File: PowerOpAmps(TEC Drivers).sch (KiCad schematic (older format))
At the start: 23 parts, among them U4 OPA569AIDWPR, U5 OPA569AIDWPR

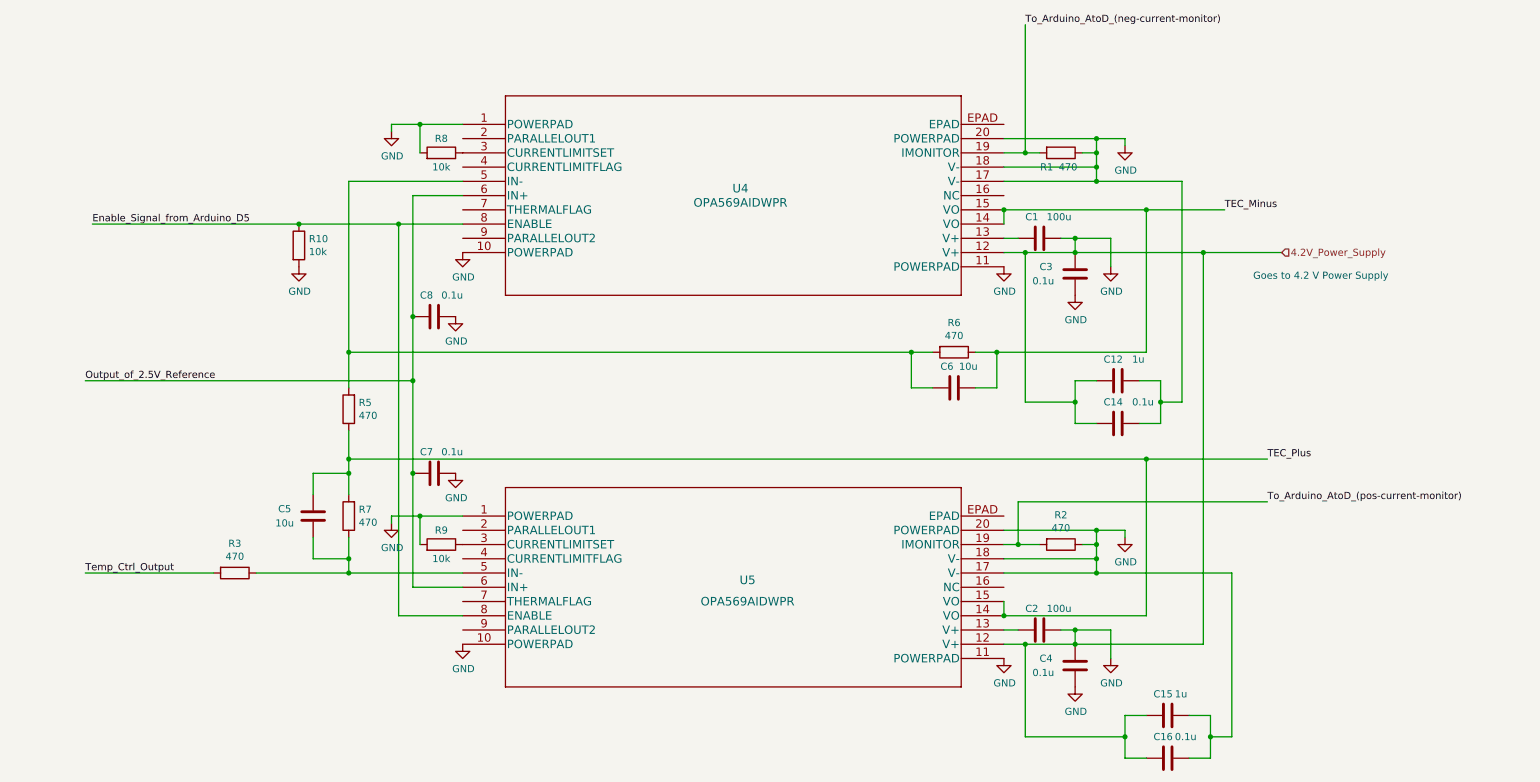
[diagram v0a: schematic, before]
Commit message: annotate all sheets
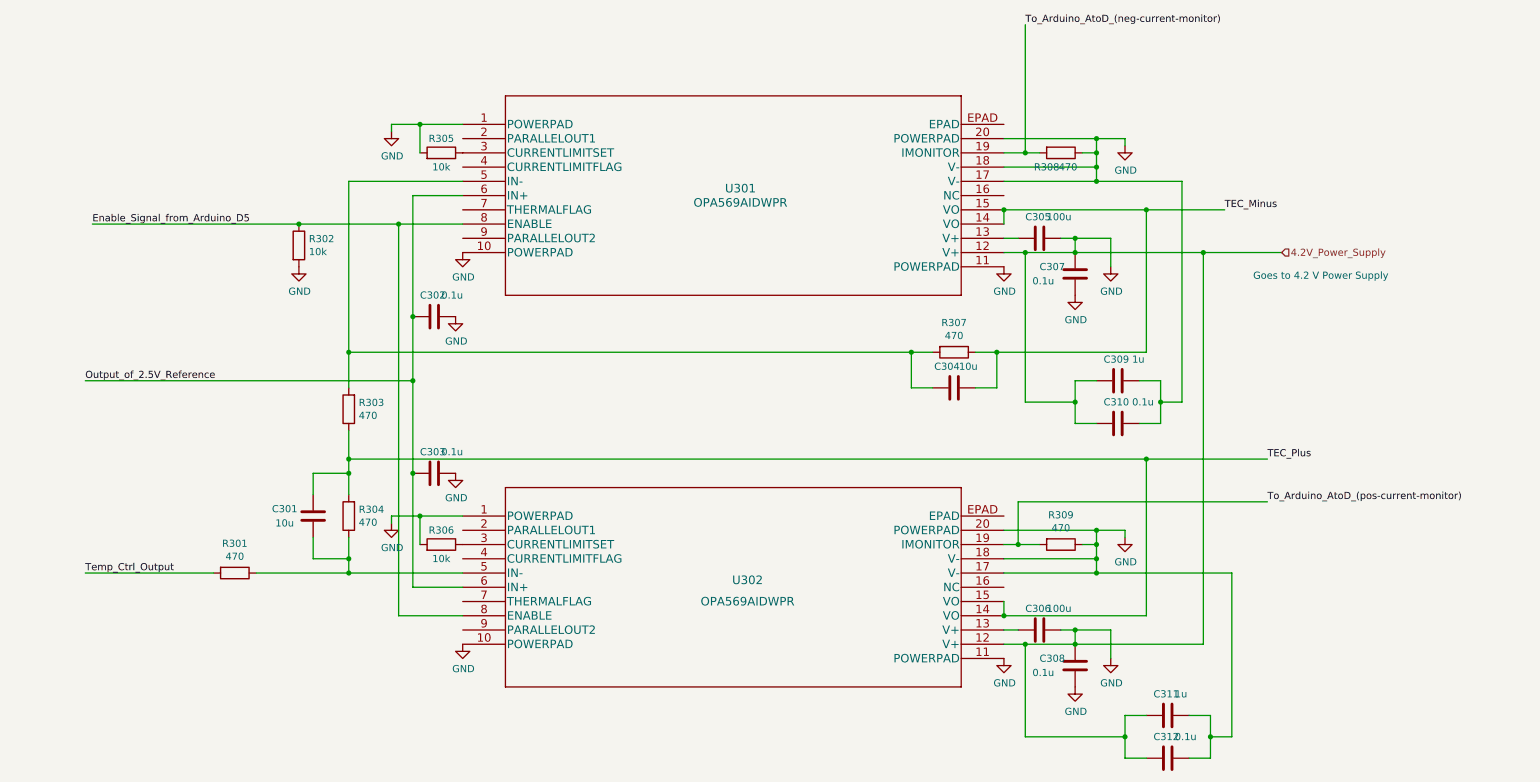
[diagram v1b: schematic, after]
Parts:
- renumbered C5 to C301, C8 to C302, C7 to C303, C6 to C304, C1 to C305, C2 to C306, C3 to C307, C4 to C308, C12 to C309, C14 to C310, C15 to C311, C16 to C312, R3 to R301, R10 to R302, R5 to R303, R7 to R304, R8 to R305, R9 to R306, R6 to R307, R1 to R308, R2 to R309, U4 to U301, U5 to U302
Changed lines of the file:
@@
 $EndDescr
 $Comp
-L OPA569AIDWPR:OPA569AIDWPR U5
+L OPA569AIDWPR:OPA569AIDWPR U302
 U 1 1 60C94364
 P 3700 4550
-F 0 "U5" H 5700 4100 60  0000 C CNN
+F 0 "U302" H 5700 4100 60  0000 C CNN
 F 1 "OPA569AIDWPR" H 5700 3950 60  0000 C CNN
 F 2 "DWP20_4P32X3P81" H 5600 4790 60  0001 C CNN
@@
 	3200 1800 3200 1850
 $Comp
-L power:GND #PWR018
+L power:GND #PWR0302
 U 1 1 60C996D8
 P 3200 1850
-F 0 "#PWR018" H 3200 1600 50  0001 C CNN
+F 0 "#PWR0302" H 3200 1600 50  0001 C CNN
 F 1 "GND" H 3205 1677 50  0000 C CNN
 F 2 "" H 3200 1850 50  0001 C CNN
@@
 	8150 2100 8150 2000
 $Comp
-L power:GND #PWR030
+L power:GND #PWR0314
 U 1 1 60C9A1CF
 P 8350 1950
-F 0 "#PWR030" H 8350 1700 50  0001 C CNN
+F 0 "#PWR0314" H 8350 1700 50  0001 C CNN
 F 1 "GND" H 8355 1777 50  0000 C CNN
 F 2 "" H 8350 1950 50  0001 C CNN
@@
 	8150 2000 8150 1900
 $Comp
-L Device:R R1
+L Device:R R308
 U 1 1 60C9D180
 P 7900 2000
-F 0 "R1" V 8000 1900 50  0000 C CNN
+F 0 "R308" V 8000 1900 50  0000 C CNN
 F 1 "470" V 8000 2050 50  0000 C CNN
 F 2 "" V 7830 2000 50  0001 C CNN
@@
 Connection ~ 8000 2600
 $Comp
-L power:GND #PWR026
+L power:GND #PWR0310
 U 1 1 60C9E215
 P 8000 3000
-F 0 "#PWR026" H 8000 2750 50  0001 C CNN
+F 0 "#PWR0310" H 8000 2750 50  0001 C CNN
 F 1 "GND" H 8005 2827 50  0000 C CNN
 F 2 "" H 8000 3000 50  0001 C CNN
@@
 $EndComp
 $Comp
-L power:GND #PWR028
+L power:GND #PWR0312
 U 1 1 60C9E30F
 P 8250 2800
-F 0 "#PWR028" H 8250 2550 50  0001 C CNN
+F 0 "#PWR0312" H 8250 2550 50  0001 C CNN
 F 1 "GND" H 8255 2627 50  0000 C CNN
 F 2 "" H 8250 2800 50  0001 C CNN
@@
 $EndComp
 $Comp
-L Device:C C3
+L Device:C C307
 U 1 1 60C9E72B
 P 8000 2850
-F 0 "C3" H 7750 2900 50  0000 L CNN
+F 0 "C307" H 7750 2900 50  0000 L CNN
 F 1 "0.1u" H 7700 2800 50  0000 L CNN
 F 2 "" H 8038 2700 50  0001 C CNN
@@
 Connection ~ 8000 2700
 $Comp
-L power:GND #PWR024
+L power:GND #PWR0308
 U 1 1 60C9EDCF
 P 7500 2800
-F 0 "#PWR024" H 7500 2550 50  0001 C CNN
+F 0 "#PWR0308" H 7500 2550 50  0001 C CNN
 F 1 "GND" H 7505 2627 50  0000 C CNN
 F 2 "" H 7500 2800 50  0001 C CNN
@@
 $EndComp
 $Comp
-L Device:C C1
+L Device:C C305
 U 1 1 60CA0405
 P 7750 2600
-F 0 "C1" V 7600 2500 50  0000 L CNN
+F 0 "C305" V 7600 2500 50  0000 L CNN
 F 1 "100u" V 7600 2650 50  0000 L CNN
 F 2 "" H 7788 2450 50  0001 C CNN
@@
 Connection ~ 8500 2400
 $Comp
-L Device:R R6
+L Device:R R307
 U 1 1 60CA6672
 P 7150 3400
-F 0 "R6" V 6943 3400 50  0000 C CNN
+F 0 "R307" V 6943 3400 50  0000 C CNN
 F 1 "470" V 7034 3400 50  0000 C CNN
 F 2 "" V 7080 3400 50  0001 C CNN
@@
 	7450 3400 7300 3400
 $Comp
-L Device:C C6
+L Device:C C304
 U 1 1 60CADB61
 P 7150 3650
-F 0 "C6" V 7000 3600 50  0000 C CNN
+F 0 "C304" V 7000 3600 50  0000 C CNN
 F 1 "10u" V 7000 3750 50  0000 C CNN
 F 2 "" H 7188 3500 50  0001 C CNN
@@
 Connection ~ 2900 3400
 $Comp
-L Device:R R5
+L Device:R R303
 U 1 1 60CAF386
 P 2900 3800
-F 0 "R5" H 2830 3754 50  0000 R CNN
+F 0 "R303" H 2830 3754 50  0000 R CNN
 F 1 "470" H 2830 3845 50  0000 R CNN
 F 2 "" V 2830 3800 50  0001 C CNN
@@
 	2650 4700 2650 4850
 $Comp
-L Device:C C5
+L Device:C C301
 U 1 1 60CB3BC7
 P 2650 4550
-F 0 "C5" H 2850 4500 50  0000 C CNN
+F 0 "C301" H 2850 4500 50  0000 C CNN
 F 1 "10u" H 2850 4600 50  0000 C CNN
 F 2 "" H 2688 4400 50  0001 C CNN
@@
 	2650 4400 2650 4250
 $Comp
-L Device:R R7
+L Device:R R304
 U 1 1 60CB4975
 P 2900 4550
-F 0 "R7" H 2830 4504 50  0000 R CNN
+F 0 "R304" H 2830 4504 50  0000 R CNN
 F 1 "470" H 2830 4595 50  0000 R CNN
 F 2 "" V 2830 4550 50  0001 C CNN
@@
 Connection ~ 2900 4950
 $Comp
-L Device:R R3
+L Device:R R301
 U 1 1 60CB799D
 P 2100 4950
-F 0 "R3" V 1893 4950 50  0000 C CNN
+F 0 "R301" V 1893 4950 50  0000 C CNN
 F 1 "470" V 1984 4950 50  0000 C CNN
 F 2 "" V 2030 4950 50  0001 C CNN
@@
 	3350 2300 3350 3150
 $Comp
-L Device:C C8
+L Device:C C302
 U 1 1 60CB9EEA
 P 3500 3150
-F 0 "C8" V 3350 3050 50  0000 L CNN
+F 0 "C302" V 3350 3050 50  0000 L CNN
 F 1 "0.1u" V 3350 3200 50  0000 L CNN
 F 2 "" H 3538 3000 50  0001 C CNN
@@
 Connection ~ 7500 2400
 $Comp
-L OPA569AIDWPR:OPA569AIDWPR U4
+L OPA569AIDWPR:OPA569AIDWPR U301
 U 1 1 60C92272
 P 3700 1800
-F 0 "U4" H 5650 1350 60  0000 C CNN
+F 0 "U301" H 5650 1350 60  0000 C CNN
 F 1 "OPA569AIDWPR" H 5650 1250 60  0000 C CNN
 F 2 "DWP20_4P32X3P81" H 5600 2040 60  0001 C CNN
@@
 $EndComp
 $Comp
-L power:GND #PWR020
+L power:GND #PWR0306
 U 1 1 60CB8330
 P 3700 2700
-F 0 "#PWR020" H 3700 2450 50  0001 C CNN
+F 0 "#PWR0306" H 3700 2450 50  0001 C CNN
 F 1 "GND" H 3705 2527 50  0000 C CNN
 F 2 "" H 3700 2700 50  0001 C CNN
@@
 	7500 2200 8150 2200
 $Comp
-L power:GND #PWR021
+L power:GND #PWR0304
 U 1 1 60CBC7D5
 P 3650 3150
-F 0 "#PWR021" H 3650 2900 50  0001 C CNN
+F 0 "#PWR0304" H 3650 2900 50  0001 C CNN
 F 1 "GND" H 3655 2977 50  0000 C CNN
 F 2 "" H 3650 3150 50  0001 C CNN
@@
 $EndComp
 $Comp
-L Device:C C7
+L Device:C C303
 U 1 1 60C859CC
 P 3500 4250
-F 0 "C7" V 3350 4150 50  0000 L CNN
+F 0 "C303" V 3350 4150 50  0000 L CNN
 F 1 "0.1u" V 3350 4300 50  0000 L CNN
 F 2 "" H 3538 4100 50  0001 C CNN
@@
 $EndComp
 $Comp
-L power:GND #PWR022
+L power:GND #PWR0305
 U 1 1 60C85B5A
 P 3650 4250
-F 0 "#PWR022" H 3650 4000 50  0001 C CNN
+F 0 "#PWR0305" H 3650 4000 50  0001 C CNN
 F 1 "GND" H 3655 4077 50  0000 C CNN
 F 2 "" H 3650 4250 50  0001 C CNN
@@
 Connection ~ 8000 5350
 $Comp
-L power:GND #PWR027
+L power:GND #PWR0311
 U 1 1 60C89B9A
 P 8000 5750
-F 0 "#PWR027" H 8000 5500 50  0001 C CNN
+F 0 "#PWR0311" H 8000 5500 50  0001 C CNN
 F 1 "GND" H 8005 5577 50  0000 C CNN
 F 2 "" H 8000 5750 50  0001 C CNN
@@
 $EndComp
 $Comp
-L power:GND #PWR029
+L power:GND #PWR0313
 U 1 1 60C89BA4
 P 8250 5550
-F 0 "#PWR029" H 8250 5300 50  0001 C CNN
+F 0 "#PWR0313" H 8250 5300 50  0001 C CNN
 F 1 "GND" H 8255 5377 50  0000 C CNN
 F 2 "" H 8250 5550 50  0001 C CNN
@@
 $EndComp
 $Comp
-L Device:C C4
+L Device:C C308
 U 1 1 60C89BAE
 P 8000 5600
-F 0 "C4" H 7750 5650 50  0000 L CNN
+F 0 "C308" H 7750 5650 50  0000 L CNN
 F 1 "0.1u" H 7700 5550 50  0000 L CNN
 F 2 "" H 8038 5450 50  0001 C CNN
@@
 Connection ~ 8000 5450
 $Comp
-L Device:C C2
+L Device:C C306
 U 1 1 60C89BB9
 P 7750 5350
-F 0 "C2" V 7600 5250 50  0000 L CNN
+F 0 "C306" V 7600 5250 50  0000 L CNN
 F 1 "100u" V 7600 5400 50  0000 L CNN
 F 2 "" H 7788 5200 50  0001 C CNN
@@
 	8900 5450 8900 2700
 $Comp
-L power:GND #PWR025
+L power:GND #PWR0309
 U 1 1 60C94EDB
 P 7500 5550
-F 0 "#PWR025" H 7500 5300 50  0001 C CNN
+F 0 "#PWR0309" H 7500 5300 50  0001 C CNN
 F 1 "GND" H 7505 5377 50  0000 C CNN
 F 2 "" H 7500 5550 50  0001 C CNN
@@
 	8150 4850 8150 4750
 $Comp
-L power:GND #PWR031
+L power:GND #PWR0315
 U 1 1 60C9936E
 P 8350 4700
-F 0 "#PWR031" H 8350 4450 50  0001 C CNN
+F 0 "#PWR0315" H 8350 4450 50  0001 C CNN
 F 1 "GND" H 8355 4527 50  0000 C CNN
 F 2 "" H 8350 4700 50  0001 C CNN
@@
 	8150 4750 8150 4650
 $Comp
-L Device:R R2
+L Device:R R309
 U 1 1 60C9937F
 P 7900 4750
-F 0 "R2" V 7693 4750 50  0000 C CNN
+F 0 "R309" V 7693 4750 50  0000 C CNN
 F 1 "470" V 7784 4750 50  0000 C CNN
 F 2 "" V 7830 4750 50  0001 C CNN
@@
 Enable_Signal_from_Arduino_D5
 $Comp
-L Device:R R10
+L Device:R R302
 U 1 1 60CB8623
 P 2550 2650
-F 0 "R10" H 2620 2696 50  0000 L CNN
+F 0 "R302" H 2620 2696 50  0000 L CNN
 F 1 "10k" H 2620 2605 50  0000 L CNN
 F 2 "" V 2480 2650 50  0001 C CNN
@@
 	2550 2500 1100 2500
 $Comp
-L power:GND #PWR017
+L power:GND #PWR0301
 U 1 1 60CB8F3D
 P 2550 2800
-F 0 "#PWR017" H 2550 2550 50  0001 C CNN
+F 0 "#PWR0301" H 2550 2550 50  0001 C CNN
 F 1 "GND" H 2555 2627 50  0000 C CNN
 F 2 "" H 2550 2800 50  0001 C CNN
@@
 $EndComp
 $Comp
-L power:GND #PWR023
+L power:GND #PWR0307
 U 1 1 60CB936E
 P 3700 5450
-F 0 "#PWR023" H 3700 5200 50  0001 C CNN
+F 0 "#PWR0307" H 3700 5200 50  0001 C CNN
 F 1 "GND" H 3705 5277 50  0000 C CNN
 F 2 "" H 3700 5450 50  0001 C CNN
@@
 	7650 5450 8000 5450
 $Comp
-L Device:C C15
+L Device:C C311
 U 1 1 60CD3EBB
 P 8650 5950
-F 0 "C15" V 8500 5850 50  0000 L CNN
+F 0 "C311" V 8500 5850 50  0000 L CNN
 F 1 "1u" V 8500 6000 50  0000 L CNN
 F 2 "" H 8688 5800 50  0001 C CNN
@@
 $EndComp
 $Comp
-L Device:C C16
+L Device:C C312
 U 1 1 60CD4799
 P 8650 6250
-F 0 "C16" V 8500 6150 50  0000 L CNN
+F 0 "C312" V 8500 6150 50  0000 L CNN
 F 1 "0.1u" V 8500 6300 50  0000 L CNN
 F 2 "" H 8688 6100 50  0001 C CNN
@@
 	8000 3600 8150 3600
 $Comp
-L Device:C C12
+L Device:C C309
 U 1 1 60CDE792
 P 8300 3600
-F 0 "C12" V 8150 3500 50  0000 L CNN
+F 0 "C309" V 8150 3500 50  0000 L CNN
 F 1 "1u" V 8150 3700 50  0000 L CNN
 F 2 "" H 8338 3450 50  0001 C CNN
@@
 $EndComp
 $Comp
-L Device:C C14
+L Device:C C310
 U 1 1 60CDE79C
 P 8300 3900
-F 0 "C14" V 8150 3800 50  0000 L CNN
+F 0 "C310" V 8150 3800 50  0000 L CNN
 F 1 "0.1u" V 8150 4000 50  0000 L CNN
 F 2 "" H 8338 3750 50  0001 C CNN
@@
 	3400 1800 3700 1800
 $Comp
-L Device:R R8
+L Device:R R305
 U 1 1 60DF1308
 P 3550 2000
-F 0 "R8" V 3650 2000 50  0000 C CNN
+F 0 "R305" V 3650 2000 50  0000 C CNN
 F 1 "10k" V 3450 2000 50  0000 C CNN
 F 2 "" V 3480 2000 50  0001 C CNN
@@
 	3200 4550 3200 4600
 $Comp
-L power:GND #PWR?
+L power:GND #PWR0303
 U 1 1 60E59C67
 P 3200 4600
-F 0 "#PWR?" H 3200 4350 50  0001 C CNN
+F 0 "#PWR0303" H 3200 4350 50  0001 C CNN
 F 1 "GND" H 3205 4427 50  0000 C CNN
 F 2 "" H 3200 4600 50  0001 C CNN
@@
 	3400 4550 3700 4550
 $Comp
-L Device:R R9
+L Device:R R306
 U 1 1 60E59C71
 P 3550 4750
-F 0 "R9" V 3650 4750 50  0000 C CNN
+F 0 "R306" V 3650 4750 50  0000 C CNN
 F 1 "10k" V 3450 4750 50  0000 C CNN
 F 2 "" V 3480 4750 50  0001 C CNN

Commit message: add footprints 2 julia
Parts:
- U301, U302: footprint DWP20_4P32X3P81 -> footprint libraries:OPA569AIDWPR
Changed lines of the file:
@@
 F 0 "U302" H 5700 4100 60  0000 C CNN
 F 1 "OPA569AIDWPR" H 5700 3950 60  0000 C CNN
-F 2 "DWP20_4P32X3P81" H 5600 4790 60  0001 C CNN
+F 2 "footprint libraries:OPA569AIDWPR" H 5600 4790 60  0001 C CNN
 F 3 "" H 3700 4550 60  0000 C CNN
 	1    3700 4550
@@
 F 0 "U301" H 5650 1350 60  0000 C CNN
 F 1 "OPA569AIDWPR" H 5650 1250 60  0000 C CNN
-F 2 "DWP20_4P32X3P81" H 5600 2040 60  0001 C CNN
+F 2 "footprint libraries:OPA569AIDWPR" H 5600 2040 60  0001 C CNN
 F 3 "" H 3700 1800 60  0000 C CNN
 	1    3700 1800

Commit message: added vishay dude & capacitor & resistor footprints
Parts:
- C301, C302, C303, C304, C305, C306, C307, C308, C309, C310, C311, C312: footprint (none) -> Capacitor_SMD:C_0402_1005Metric
- R301, R302, R303, R304, R305, R306, R307, R308, R309: footprint (none) -> Resistor_SMD:R_0402_1005Metric
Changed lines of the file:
@@
 F 0 "R308" V 8000 1900 50  0000 C CNN
 F 1 "470" V 8000 2050 50  0000 C CNN
-F 2 "" V 7830 2000 50  0001 C CNN
+F 2 "Resistor_SMD:R_0402_1005Metric" V 7830 2000 50  0001 C CNN
 F 3 "~" H 7900 2000 50  0001 C CNN
 	1    7900 2000
@@
 F 0 "C307" H 7750 2900 50  0000 L CNN
 F 1 "0.1u" H 7700 2800 50  0000 L CNN
-F 2 "" H 8038 2700 50  0001 C CNN
+F 2 "Capacitor_SMD:C_0402_1005Metric" H 8038 2700 50  0001 C CNN
 F 3 "~" H 8000 2850 50  0001 C CNN
 	1    8000 2850
@@
 F 0 "C305" V 7600 2500 50  0000 L CNN
 F 1 "100u" V 7600 2650 50  0000 L CNN
-F 2 "" H 7788 2450 50  0001 C CNN
+F 2 "Capacitor_SMD:C_0402_1005Metric" H 7788 2450 50  0001 C CNN
 F 3 "~" H 7750 2600 50  0001 C CNN
 	1    7750 2600
@@
 F 0 "R307" V 6943 3400 50  0000 C CNN
 F 1 "470" V 7034 3400 50  0000 C CNN
-F 2 "" V 7080 3400 50  0001 C CNN
+F 2 "Resistor_SMD:R_0402_1005Metric" V 7080 3400 50  0001 C CNN
 F 3 "~" H 7150 3400 50  0001 C CNN
 	1    7150 3400
@@
 F 0 "C304" V 7000 3600 50  0000 C CNN
 F 1 "10u" V 7000 3750 50  0000 C CNN
-F 2 "" H 7188 3500 50  0001 C CNN
+F 2 "Capacitor_SMD:C_0402_1005Metric" H 7188 3500 50  0001 C CNN
 F 3 "~" H 7150 3650 50  0001 C CNN
 	1    7150 3650
@@
 F 0 "R303" H 2830 3754 50  0000 R CNN
 F 1 "470" H 2830 3845 50  0000 R CNN
-F 2 "" V 2830 3800 50  0001 C CNN
+F 2 "Resistor_SMD:R_0402_1005Metric" V 2830 3800 50  0001 C CNN
 F 3 "~" H 2900 3800 50  0001 C CNN
 	1    2900 3800
@@
 F 0 "C301" H 2850 4500 50  0000 C CNN
 F 1 "10u" H 2850 4600 50  0000 C CNN
-F 2 "" H 2688 4400 50  0001 C CNN
+F 2 "Capacitor_SMD:C_0402_1005Metric" H 2688 4400 50  0001 C CNN
 F 3 "~" H 2650 4550 50  0001 C CNN
 	1    2650 4550
@@
 F 0 "R304" H 2830 4504 50  0000 R CNN
 F 1 "470" H 2830 4595 50  0000 R CNN
-F 2 "" V 2830 4550 50  0001 C CNN
+F 2 "Resistor_SMD:R_0402_1005Metric" V 2830 4550 50  0001 C CNN
 F 3 "~" H 2900 4550 50  0001 C CNN
 	1    2900 4550
@@
 F 0 "R301" V 1893 4950 50  0000 C CNN
 F 1 "470" V 1984 4950 50  0000 C CNN
-F 2 "" V 2030 4950 50  0001 C CNN
+F 2 "Resistor_SMD:R_0402_1005Metric" V 2030 4950 50  0001 C CNN
 F 3 "~" H 2100 4950 50  0001 C CNN
 	1    2100 4950
@@
 F 0 "C302" V 3350 3050 50  0000 L CNN
 F 1 "0.1u" V 3350 3200 50  0000 L CNN
-F 2 "" H 3538 3000 50  0001 C CNN
+F 2 "Capacitor_SMD:C_0402_1005Metric" H 3538 3000 50  0001 C CNN
 F 3 "~" H 3500 3150 50  0001 C CNN
 	1    3500 3150
@@
 F 0 "C303" V 3350 4150 50  0000 L CNN
 F 1 "0.1u" V 3350 4300 50  0000 L CNN
-F 2 "" H 3538 4100 50  0001 C CNN
+F 2 "Capacitor_SMD:C_0402_1005Metric" H 3538 4100 50  0001 C CNN
 F 3 "~" H 3500 4250 50  0001 C CNN
 	1    3500 4250
@@
 F 0 "C308" H 7750 5650 50  0000 L CNN
 F 1 "0.1u" H 7700 5550 50  0000 L CNN
-F 2 "" H 8038 5450 50  0001 C CNN
+F 2 "Capacitor_SMD:C_0402_1005Metric" H 8038 5450 50  0001 C CNN
 F 3 "~" H 8000 5600 50  0001 C CNN
 	1    8000 5600
@@
 F 0 "C306" V 7600 5250 50  0000 L CNN
 F 1 "100u" V 7600 5400 50  0000 L CNN
-F 2 "" H 7788 5200 50  0001 C CNN
+F 2 "Capacitor_SMD:C_0402_1005Metric" H 7788 5200 50  0001 C CNN
 F 3 "~" H 7750 5350 50  0001 C CNN
 	1    7750 5350
@@
 F 0 "R309" V 7693 4750 50  0000 C CNN
 F 1 "470" V 7784 4750 50  0000 C CNN
-F 2 "" V 7830 4750 50  0001 C CNN
+F 2 "Resistor_SMD:R_0402_1005Metric" V 7830 4750 50  0001 C CNN
 F 3 "~" H 7900 4750 50  0001 C CNN
 	1    7900 4750
@@
 F 0 "R302" H 2620 2696 50  0000 L CNN
 F 1 "10k" H 2620 2605 50  0000 L CNN
-F 2 "" V 2480 2650 50  0001 C CNN
+F 2 "Resistor_SMD:R_0402_1005Metric" V 2480 2650 50  0001 C CNN
 F 3 "~" H 2550 2650 50  0001 C CNN
 	1    2550 2650
@@
 F 0 "C311" V 8500 5850 50  0000 L CNN
 F 1 "1u" V 8500 6000 50  0000 L CNN
-F 2 "" H 8688 5800 50  0001 C CNN
+F 2 "Capacitor_SMD:C_0402_1005Metric" H 8688 5800 50  0001 C CNN
 F 3 "~" H 8650 5950 50  0001 C CNN
 	1    8650 5950
@@
 F 0 "C312" V 8500 6150 50  0000 L CNN
 F 1 "0.1u" V 8500 6300 50  0000 L CNN
-F 2 "" H 8688 6100 50  0001 C CNN
+F 2 "Capacitor_SMD:C_0402_1005Metric" H 8688 6100 50  0001 C CNN
 F 3 "~" H 8650 6250 50  0001 C CNN
 	1    8650 6250
@@
 F 0 "C309" V 8150 3500 50  0000 L CNN
 F 1 "1u" V 8150 3700 50  0000 L CNN
-F 2 "" H 8338 3450 50  0001 C CNN
+F 2 "Capacitor_SMD:C_0402_1005Metric" H 8338 3450 50  0001 C CNN
 F 3 "~" H 8300 3600 50  0001 C CNN
 	1    8300 3600
@@
 F 0 "C310" V 8150 3800 50  0000 L CNN
 F 1 "0.1u" V 8150 4000 50  0000 L CNN
-F 2 "" H 8338 3750 50  0001 C CNN
+F 2 "Capacitor_SMD:C_0402_1005Metric" H 8338 3750 50  0001 C CNN
 F 3 "~" H 8300 3900 50  0001 C CNN
 	1    8300 3900
@@
 F 0 "R305" V 3650 2000 50  0000 C CNN
 F 1 "10k" V 3450 2000 50  0000 C CNN
-F 2 "" V 3480 2000 50  0001 C CNN
+F 2 "Resistor_SMD:R_0402_1005Metric" V 3480 2000 50  0001 C CNN
 F 3 "~" H 3550 2000 50  0001 C CNN
 	1    3550 2000
@@
 F 0 "R306" V 3650 4750 50  0000 C CNN
 F 1 "10k" V 3450 4750 50  0000 C CNN
-F 2 "" V 3480 4750 50  0001 C CNN
+F 2 "Resistor_SMD:R_0402_1005Metric" V 3480 4750 50  0001 C CNN
 F 3 "~" H 3550 4750 50  0001 C CNN
 	1    3550 4750

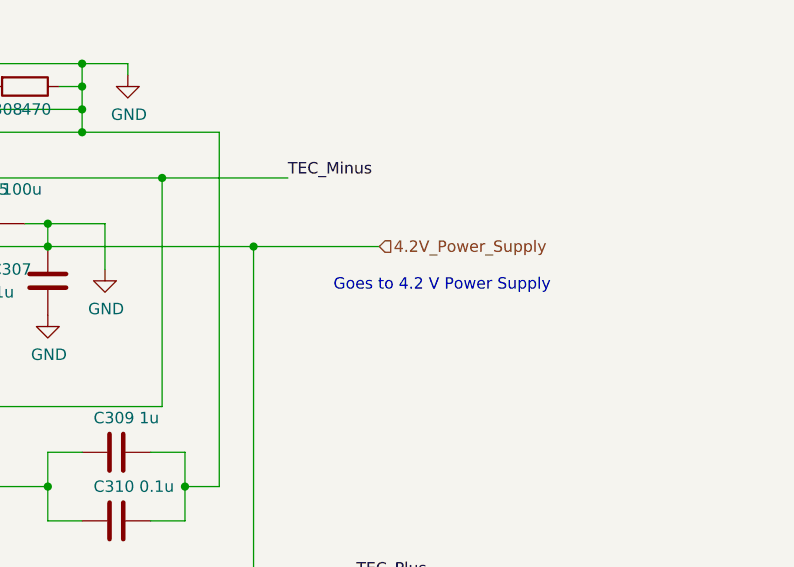
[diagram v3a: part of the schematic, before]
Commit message: added more ports
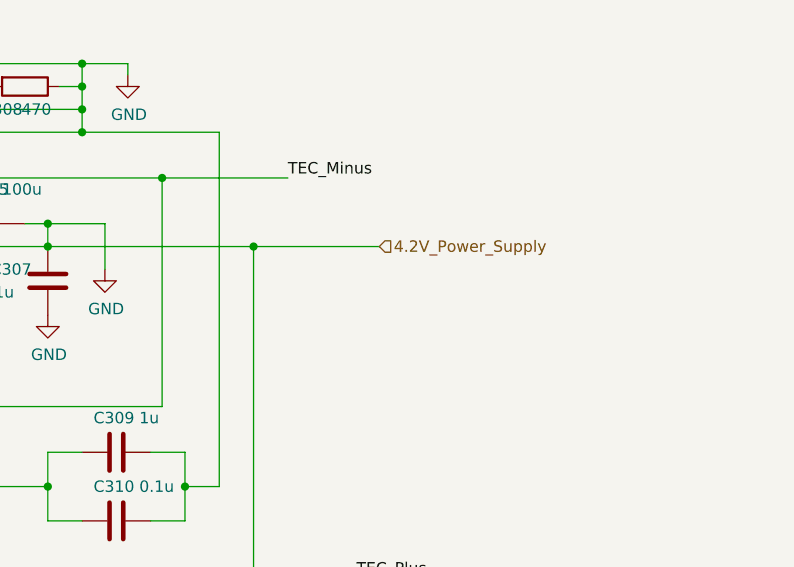
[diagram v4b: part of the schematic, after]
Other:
- note removed: "Goes to 4.2 V Power Supply\n"
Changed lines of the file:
@@
 	0    1    -1   0
 $EndComp
-Text Notes 10200 2900 2    50   ~ 0
-Goes to 4.2 V Power Supply\n
 Text HLabel 9450 2700 2    50   Input ~ 0
 4.2V_Power_Supply
